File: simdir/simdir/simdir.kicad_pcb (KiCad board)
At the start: 4 copper layers, 200 x 160 mm, 48 parts, among them Q1 BC847, Q2 BC847, Q3 BC847, Q4 BC847, Q5 BC847, Q6 BC847, Q7 BC847, Q8 BC847, U1 MASWSS0178, U10 MASWSS0178, U11 MASWSS0178, U12 MASWSS0178, U13 MASWSS0178, U14 MASWSS0178, U15 MASWSS0178, U16 MASWSS0178, U2 MASWSS0178, U3 MASWSS0178, U4 MASWSS0178, U5 MASWSS0178, U6 MASWSS0178, U7 MASWSS0178, U8 MASWSS0178, U9 MASWSS0178

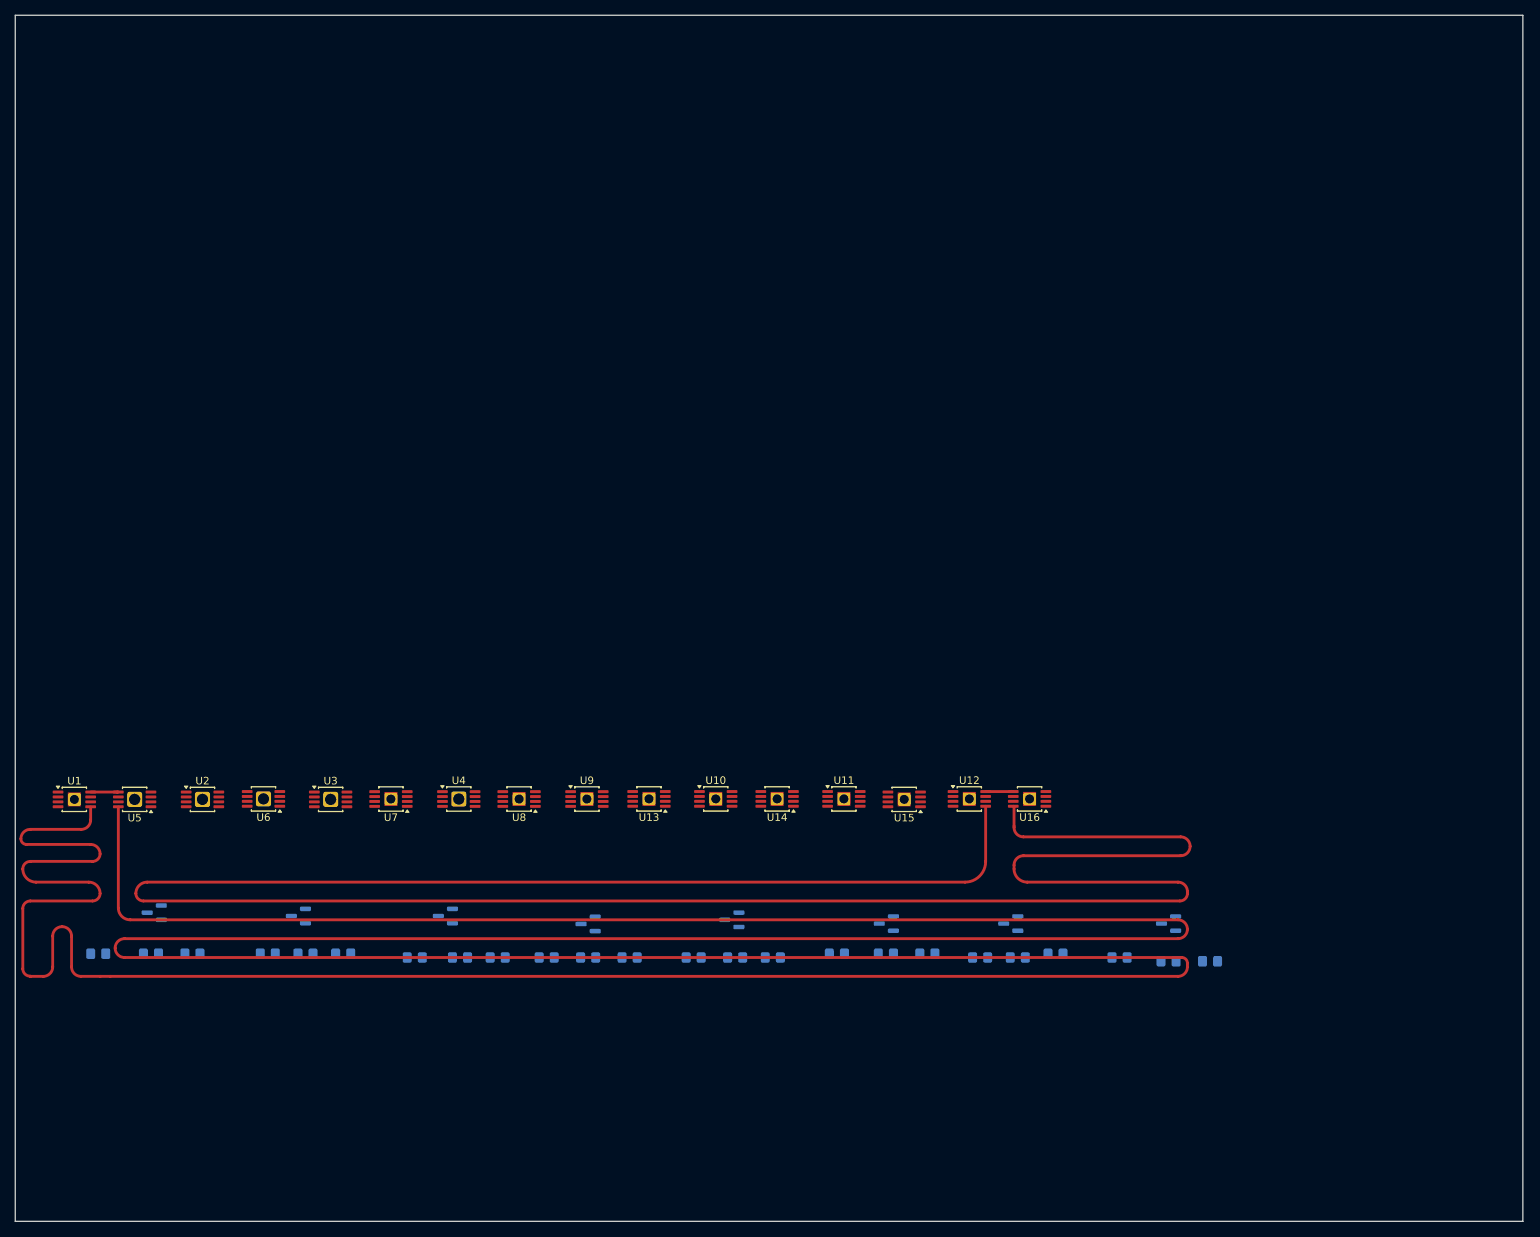
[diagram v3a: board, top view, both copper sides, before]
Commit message: Added delay meanders.
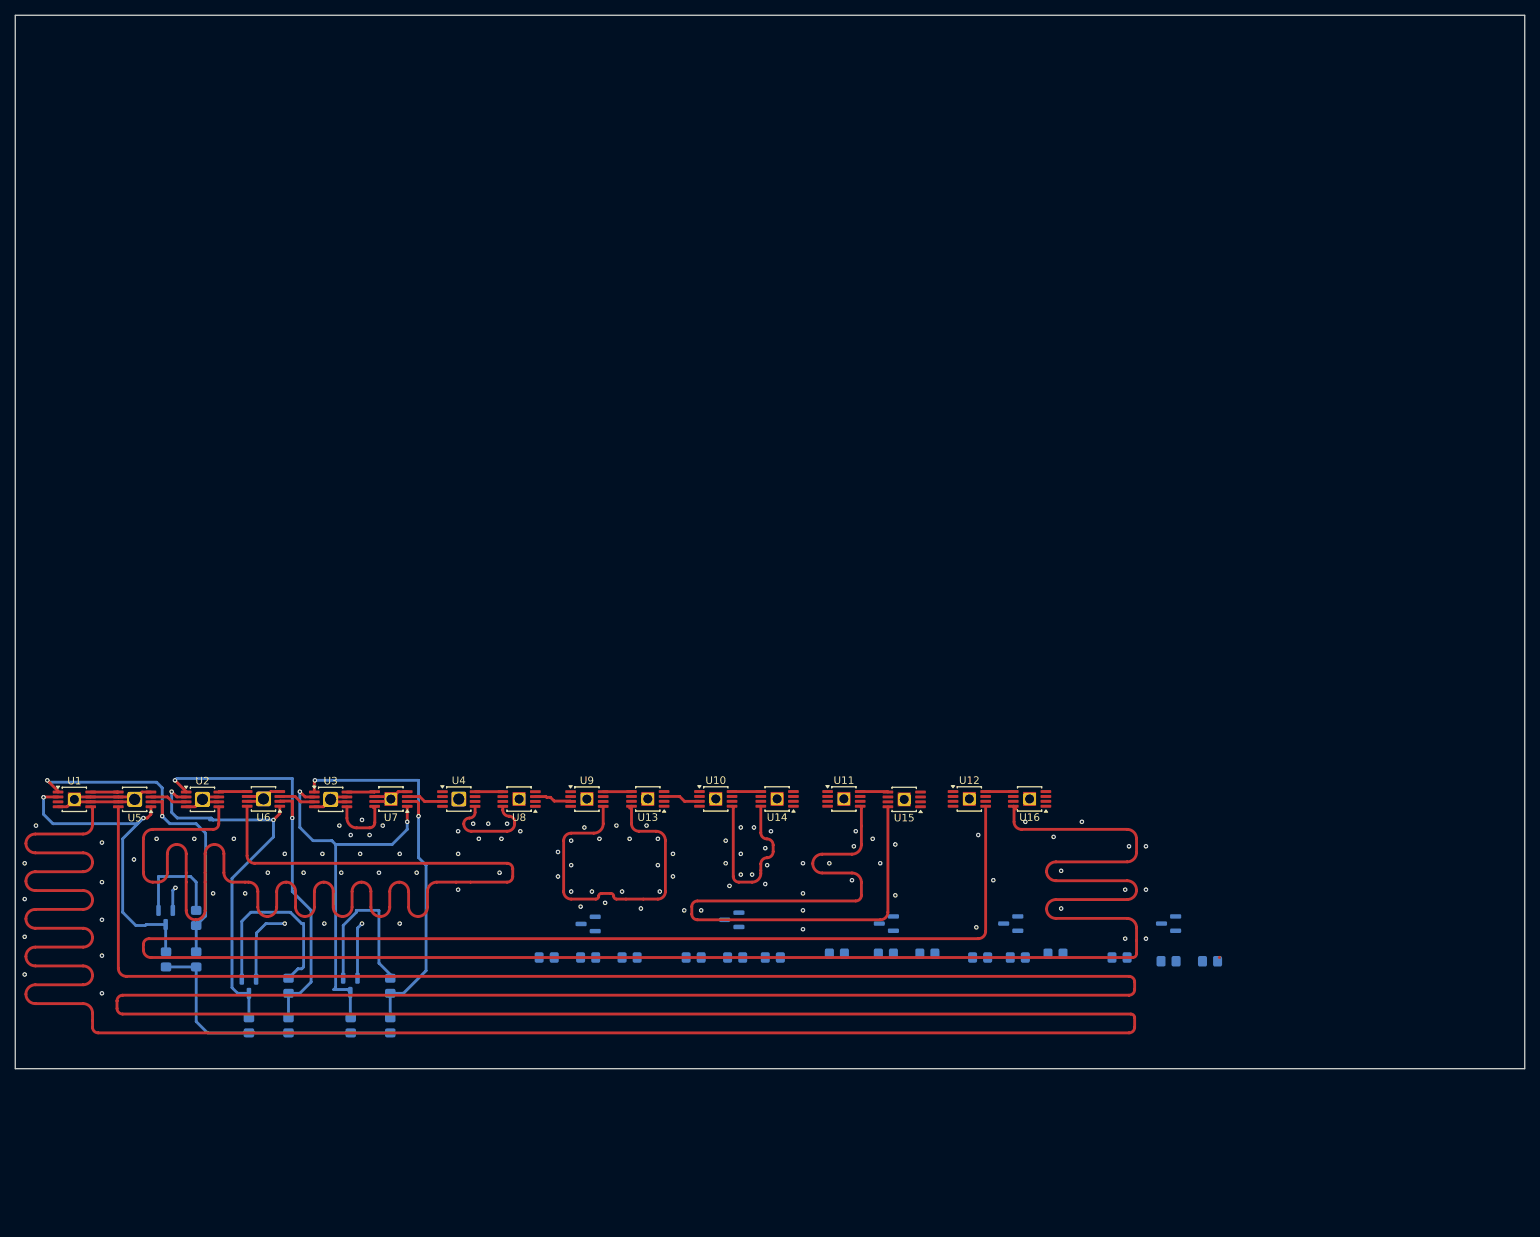
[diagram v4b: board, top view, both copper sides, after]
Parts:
- moved R9 21.5 mm to (64.5, 154.0), turned to -90 degrees
- moved R6 15.7 mm to (51.0, 154.0), turned to -90 degrees
- moved Q3 15.6 mm to (64.5, 148.7), turned to -90 degrees
- moved R1 13.0 mm to (44.0, 145.2), turned to 90 degrees
- moved Q2 11.4 mm to (51.0, 148.8), turned to -90 degrees
- moved R8 9.98 mm to (69.8, 148.8), turned to 90 degrees
- moved R4 9.89 mm to (56.2, 154.0), turned to 90 degrees
- moved R7 9.57 mm to (69.8, 154.0), turned to 90 degrees
- moved R5 4.81 mm to (56.2, 148.8), turned to 90 degrees
- moved R3 4.78 mm to (44.0, 139.8), turned to 90 degrees
- moved R2 2.14 mm to (40.0, 145.2), turned to -90 degrees
- moved Q1 1.64 mm to (40.0, 139.7), turned to -90 degrees
- moved U13 0.16 mm to (103.9, 124.0)
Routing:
- net /channel1/RF1_meander: track 0.00 -> 170.8 mm
- net /channel1/RF6_meander: track 0.00 -> 87.7 mm
- net /channel1/GND: track 0.00 -> 71.4 mm, vias 0 -> 105
- net Net-(U2-CTL1): track 0.00 -> 56.7 mm, vias 0 -> 2
- net Net-(U3-CTL1): track 0.00 -> 53.6 mm, vias 0 -> 2
- net Net-(Q2-C): track 0.00 -> 51.9 mm, vias 0 -> 2
- net Net-(Q3-C): track 0.00 -> 51.1 mm, vias 0 -> 2
- net Net-(U1-CTL1): track 0.00 -> 48.0 mm, vias 0 -> 2
- net /channel1/RF4_meander: track 0.00 -> 46.0 mm
- net Net-(Q1-C): track 0.00 -> 43.2 mm, vias 0 -> 2
- net /channel1/VCC: track 0.00 -> 37.6 mm
- net Net-(Q2-B): track 0.00 -> 25.4 mm
- net /channel1/RF5_meander: track 0.00 -> 24.7 mm
- net Net-(Q3-B): track 0.00 -> 22.3 mm
- net /channel1/RF3_meander: track 0.00 -> 14.0 mm
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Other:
- board size 200 x 160 mm -> 200.2 x 139.8 mm

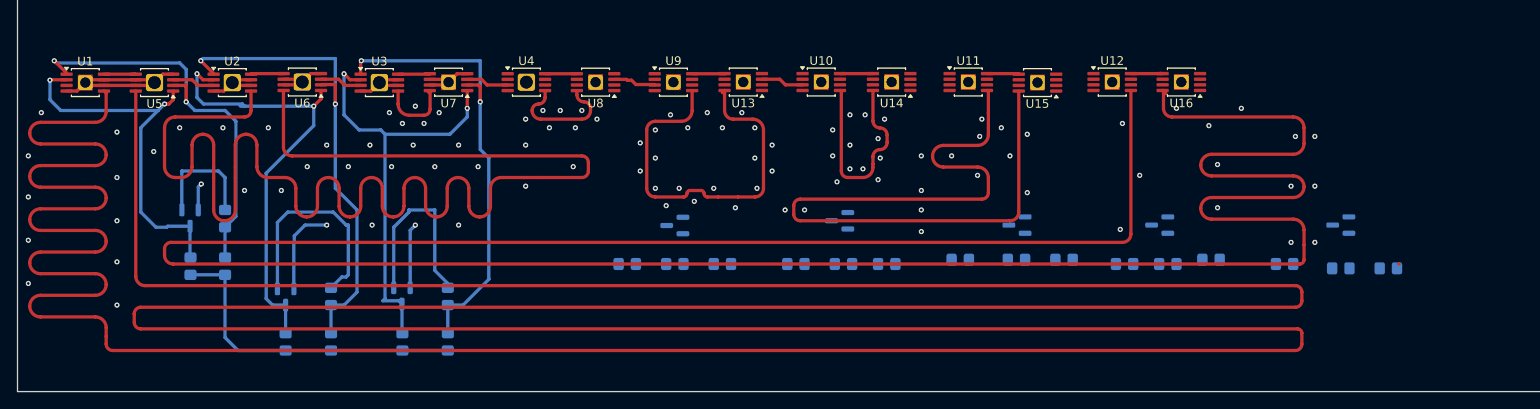
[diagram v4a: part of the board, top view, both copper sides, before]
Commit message: Routed control logic for switches.
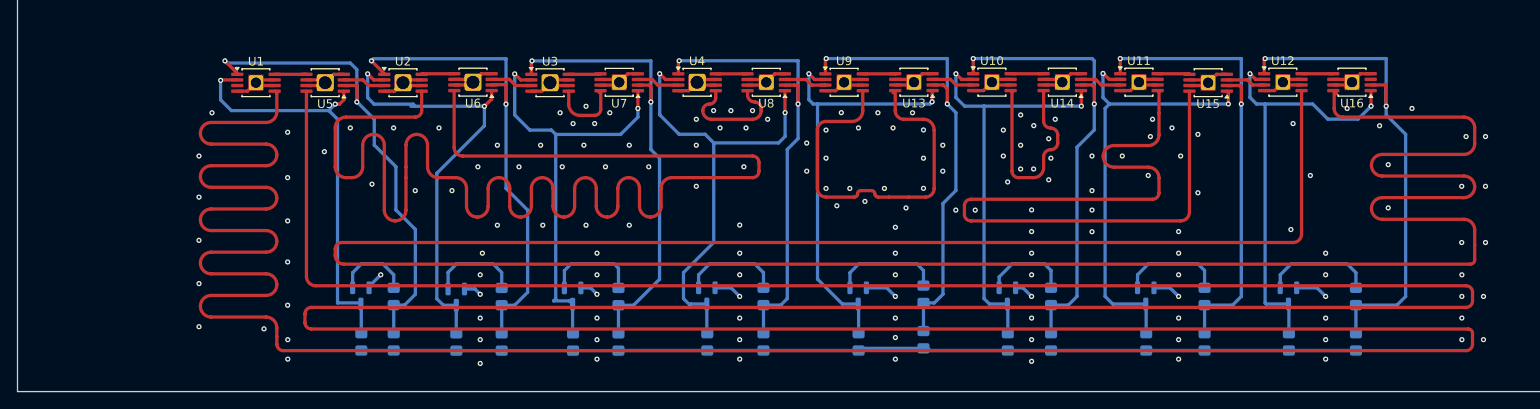
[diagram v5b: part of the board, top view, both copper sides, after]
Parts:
- moved Q1 21.7 mm to (59.7, 148.7)
- moved R2 21.6 mm to (59.8, 154.0)
- moved R3 21.5 mm to (63.5, 148.8)
- moved R1 21.4 mm to (63.5, 154.0)
- moved U12 19.7 mm to (166.3, 124.0)
- moved U14 19.7 mm to (140.8, 124.0)
- moved Q2 19.7 mm to (70.7, 148.8)
- moved Q3 19.7 mm to (84.2, 148.7)
- moved R4 19.7 mm to (76.0, 154.0)
- moved R5 19.7 mm to (76.0, 148.8)
- moved R6 19.7 mm to (70.7, 154.0)
- moved R7 19.7 mm to (89.5, 154.0)
- moved R8 19.7 mm to (89.5, 148.8)
- moved R9 19.7 mm to (84.2, 154.0)
- moved U1 19.7 mm to (47.6, 124.0)
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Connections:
- U16 pad 1: Net-(U12-CTL1) -> Net-(Q8-C)
- U16 pad 2: Net-(Q8-C) -> Net-(U12-CTL1)
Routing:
- net /channel1/VCC: track 37.6 -> 115.2 mm
- net /channel1/GND: track 71.4 -> 137.2 mm, vias 105 -> 163
- net Net-(U12-CTL1): track 0.00 -> 58.0 mm, vias 0 -> 2
- net Net-(U11-CTL1): track 0.00 -> 54.9 mm, vias 0 -> 2
- net Net-(Q4-C): track 0.00 -> 54.5 mm, vias 0 -> 2
- net Net-(U10-CTL1): track 0.00 -> 54.2 mm, vias 0 -> 2
- net Net-(U13-CTL2): track 0.00 -> 53.6 mm, vias 0 -> 2
- net Net-(U4-CTL1): track 0.00 -> 53.3 mm, vias 0 -> 2
- net Net-(Q7-C): track 0.00 -> 52.3 mm, vias 0 -> 2
- net Net-(Q8-C): track 0.00 -> 51.3 mm, vias 0 -> 2
- net Net-(Q5-C): track 0.00 -> 50.6 mm, vias 0 -> 2
- net Net-(Q6-C): track 0.00 -> 50.4 mm, vias 0 -> 2
- net Net-(Q2-B): track 25.4 -> 10.7 mm
- net Net-(Q8-B): track 0.00 -> 12.9 mm
- net Net-(Q5-B): track 0.00 -> 12.7 mm
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
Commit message: Add digital logic to channel
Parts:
- added C1: 470n, Capacitor_SMD:C_0805_2012Metric_Pad1.18x1.45mm_HandSolder, B.Cu at (192.5, 157.0)
- added C2: 470n, Capacitor_SMD:C_0805_2012Metric_Pad1.18x1.45mm_HandSolder, F.Cu at (211.0, 79.8)
- added FB1: FerriteBead, Inductor_SMD:L_0805_2012Metric_Pad1.05x1.20mm_HandSolder, B.Cu at (197.2, 157.0)
- added Q10: BC847, Package_TO_SOT_SMD:SOT-23, F.Cu at (191.5, 84.9)
- added Q11: BC847, Package_TO_SOT_SMD:SOT-23, F.Cu at (196.4, 80.5)
- added Q12: BC847, Package_TO_SOT_SMD:SOT-23, F.Cu at (196.4, 84.9)
- added Q13: BC847, Package_TO_SOT_SMD:SOT-23, F.Cu at (201.3, 80.5)
- added Q14: BC847, Package_TO_SOT_SMD:SOT-23, F.Cu at (201.3, 84.9)
- added Q15: BC847, Package_TO_SOT_SMD:SOT-23, F.Cu at (206.2, 80.5)
- added Q16: BC847, Package_TO_SOT_SMD:SOT-23, F.Cu at (206.2, 84.9)
- added Q9: BC847, Package_TO_SOT_SMD:SOT-23, F.Cu at (191.5, 80.5)
- added R25: 1k, Resistor_SMD:R_0805_2012Metric_Pad1.20x1.40mm_HandSolder, B.Cu at (207.5, 115.0)
- added R26: 1k, Resistor_SMD:R_0805_2012Metric_Pad1.20x1.40mm_HandSolder, B.Cu at (207.5, 120.0)
- added R27: 1k, Resistor_SMD:R_0805_2012Metric_Pad1.20x1.40mm_HandSolder, B.Cu at (207.5, 125.2)
- added R28: 1k, Resistor_SMD:R_0805_2012Metric_Pad1.20x1.40mm_HandSolder, B.Cu at (207.5, 130.5)
- added R29: 1k, Resistor_SMD:R_0805_2012Metric_Pad1.20x1.40mm_HandSolder, B.Cu at (207.5, 138.8)
- added R30: 1k, Resistor_SMD:R_0805_2012Metric_Pad1.20x1.40mm_HandSolder, B.Cu at (207.5, 143.8)
- added R31: 1k, Resistor_SMD:R_0805_2012Metric_Pad1.20x1.40mm_HandSolder, B.Cu at (207.2, 148.8)
- added R32: 1k, Resistor_SMD:R_0805_2012Metric_Pad1.20x1.40mm_HandSolder, B.Cu at (207.2, 153.8)
- added R33: 4.7k, Resistor_SMD:R_0805_2012Metric_Pad1.20x1.40mm_HandSolder, F.Cu at (242.0, 102.0)
- added R34: 4.7k, Resistor_SMD:R_0805_2012Metric_Pad1.20x1.40mm_HandSolder, F.Cu at (242.0, 107.5)
- added R35: 4.7k, Resistor_SMD:R_0805_2012Metric_Pad1.20x1.40mm_HandSolder, F.Cu at (242.2, 112.8)
- added R36: 4.7k, Resistor_SMD:R_0805_2012Metric_Pad1.20x1.40mm_HandSolder, F.Cu at (242.2, 117.8)
- added R37: 4.7k, Resistor_SMD:R_0805_2012Metric_Pad1.20x1.40mm_HandSolder, F.Cu at (211.7, 88.6)
- added R38: 4.7k, Resistor_SMD:R_0805_2012Metric_Pad1.20x1.40mm_HandSolder, F.Cu at (211.7, 91.6)
- added R39: 4.7k, Resistor_SMD:R_0805_2012Metric_Pad1.20x1.40mm_HandSolder, F.Cu at (211.7, 94.5)
- added R40: 4.7k, Resistor_SMD:R_0805_2012Metric_Pad1.20x1.40mm_HandSolder, F.Cu at (211.7, 97.5)
- added SWLSB1: CTS221, hand:CTS221, F.Cu at (215.7, 126.0)
- added SWMSB1: CTS221, hand:CTS221, F.Cu at (215.9, 136.2)
- added U17: LTV-847S, Package_DIP:SMDIP-16_W9.53mm, B.Cu at (197.3, 121.4)
- added U18: LTV-847S, Package_DIP:SMDIP-16_W9.53mm, B.Cu at (197.3, 144.9)
- added U19: 74HCT595, Package_SO:SOIC-16_3.9x9.9mm_P1.27mm, F.Cu at (238.7, 136.2)
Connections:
- net /channel1/GND renamed /channel1/RF_GND
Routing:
- net Net-(U2-CTL1): track 56.7 -> 286.4 mm
- net Net-(U1-CTL1): track 56.4 -> 260.8 mm, vias 2 -> 3
- net Net-(U3-CTL1): track 53.6 -> 164.2 mm
- net /channel1/VCC: track 115.2 -> 210.7 mm, vias 0 -> 2
- net Net-(U4-CTL1): track 53.3 -> 142.8 mm
- net Net-(U13-CTL2): track 53.6 -> 139.2 mm, vias 2 -> 3
- net Net-(U10-CTL1): track 54.2 -> 108.6 mm
- net Net-(U11-CTL1): track 54.9 -> 98.1 mm
- net Net-(Q16-C): track 0.00 -> 37.0 mm
- net Net-(Q10-C): track 0.00 -> 31.6 mm, vias 0 -> 1
- net Net-(Q12-C): track 0.00 -> 28.8 mm
- net /channel1/RF_GND: track 137.2 -> 162.4 mm, vias 163 -> 167
- net Net-(Q14-C): track 0.00 -> 18.6 mm, vias 0 -> 1
- net Net-(Q9-C): track 0.00 -> 18.1 mm
- net Net-(U12-CTL1): track 58.0 -> 71.6 mm, vias 2 -> 4
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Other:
- board size 200.2 x 139.8 mm -> 230 x 139.8 mm

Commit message: Finished channel layout.
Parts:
- added J1: Conn_Coaxial, Connector_Coaxial:SMA_Amphenol_132289_EdgeMount, F.Cu at (22.9, 148.9)
- C2, Q10, Q11, Q12, Q13, Q14, Q15, Q16, Q9, R33, R34, R35, R36, R37, R38, R39, R40, U19: moved to B.Cu
- moved C2 72.8 mm to (252.2, 139.8), turned to 180 degrees
- moved Q16 70.5 mm to (230.1, 151.3), turned to 180 degrees
- moved Q15 69.9 mm to (229.9, 146.2), turned to 180 degrees
- moved Q14 63.0 mm to (229.8, 141.1), turned to 180 degrees
- moved Q13 62.6 mm to (229.8, 136.2), turned to 180 degrees
- moved R40 58.1 mm to (236.0, 150.2), turned to 180 degrees
- moved Q12 56.7 mm to (230.1, 130.4), turned to 180 degrees
- moved R39 56.3 mm to (236.0, 145.2), turned to 180 degrees
- moved Q11 56.1 mm to (230.3, 125.2), turned to 180 degrees
- moved R38 54.4 mm to (236.0, 140.2), turned to 180 degrees
- moved Q10 52.7 mm to (230.7, 120.0), turned to 180 degrees
- moved R37 52.6 mm to (236.0, 135.2), turned to 180 degrees
- moved Q9 52.3 mm to (230.6, 115.2), turned to 180 degrees
- moved R33 13.4 mm to (236.5, 114.2), turned to 180 degrees
- moved R36 13.2 mm to (236.2, 129.5), turned to 180 degrees
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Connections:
- R37 pad 1: unconnected-(R37-Pad1) -> Net-(U19-QE)
- U16 pad 3: /channel1/RF-Out -> Net-(J1-In)
- U19 pad 12: /channel1/CLK -> /channel1/RCLK
- U19 pad 4: unconnected-(U19-QE-Pad4) -> Net-(U19-QE)
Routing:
- net Net-(J1-In): track 0.00 -> 196.8 mm
- net /channel1/Dig_GND: track 0.00 -> 136.2 mm, vias 0 -> 12
- net /channel1/5v: track 0.00 -> 73.9 mm
- net Net-(U19-QA): track 0.00 -> 44.8 mm
- net /channel1/RF_GND: track 162.4 -> 196.5 mm, vias 167 -> 175
- net Net-(U19-QH): track 0.00 -> 31.9 mm, vias 0 -> 2
- net Net-(U19-QB): track 0.00 -> 31.7 mm
- net Net-(U19-QG): track 0.00 -> 26.1 mm, vias 0 -> 2
- net Net-(U19-QC): track 0.00 -> 22.7 mm
- net Net-(Q11-C): track 12.5 -> 32.4 mm, vias 0 -> 2
- net Net-(U19-QF): track 0.00 -> 19.4 mm, vias 0 -> 2
- net Net-(U19-QD): track 0.00 -> 15.2 mm, vias 0 -> 2
- net Net-(Q15-C): track 12.6 -> 27.3 mm
- net Net-(Q13-C): track 8.45 -> 22.6 mm
- net Net-(Q9-C): track 18.1 -> 32.0 mm
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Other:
- board size 230 x 139.8 mm -> 240 x 139.8 mm

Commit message: Finalized channel design.
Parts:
- added R41: 63.4, Resistor_SMD:R_0805_2012Metric_Pad1.20x1.40mm_HandSolder, F.Cu at (30.2, 148.7)
- added R42: 63.4, Resistor_SMD:R_0805_2012Metric_Pad1.20x1.40mm_HandSolder, F.Cu at (34.5, 147.0)
- added R43: 71.5, Resistor_SMD:R_0805_2012Metric_Pad1.20x1.40mm_HandSolder, F.Cu at (30.2, 145.8)
- R11, R14, R17, R20, R23, R3, R5, R8: value 4.7k -> 100k
- R33, R34, R35, R36, R37, R38, R39, R40: value 4.7k -> 10k
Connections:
- U16 pad 3: Net-(J1-In) -> Net-(U16-RFC)
- U17 pad 1: /channel1/VCC -> /channel1/5v
- U17 pad 3: /channel1/VCC -> /channel1/5v
- U17 pad 5: /channel1/VCC -> /channel1/5v
- U17 pad 7: /channel1/VCC -> /channel1/5v
- U18 pad 1: /channel1/VCC -> /channel1/5v
- U18 pad 3: /channel1/VCC -> /channel1/5v
- U18 pad 5: /channel1/VCC -> /channel1/5v
- U18 pad 7: /channel1/VCC -> /channel1/5v
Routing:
- net Net-(U16-RFC): track 0.00 -> 192.3 mm
- net Net-(J1-In): track 196.8 -> 9.43 mm
- net /channel1/VCC: track 222.1 -> 143.1 mm
- net /channel1/5v: track 73.9 -> 146.9 mm
- net /channel1/RF_GND: track 196.5 -> 199.7 mm, vias 175 -> 177
- added copper zone on B.Cu, net /channel1/5v
- added copper zone on F.Cu, net /channel1/RF_GND
